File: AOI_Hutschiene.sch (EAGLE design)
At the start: 33 parts, among them IC1 l4940, SW1 EC12E_SW

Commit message: updated design
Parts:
- removed H5, H6, H7: MOUNT-PAD-ROUND3.2, holes:MOUNT-PAD-ROUND3.2
- removed SV3: (no value), con-lsta:FE05W
- added D1: 1N4148DO35-7, diode:1N4148DO35-7
- added R5, R6: 4k7, resistor:R-EU_0207/2V
- added R7, R8: 22k, resistor:R-EU_0207/10
- added SV5: (no value), con-lstb:MA04-1
- C3: value 1000uF -> 1mF
- F2: value FUSESH22,5 -> 100mA_or_smaller
- R1, R2: value (none) -> 180
- TR1: value 6v -> 6V, 300mA
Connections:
- net N$12 renamed DSS_VCC
- removed net REL_HEAT_2: U$1.A1
- removed net REL_MIX_2: U$1.A3
- net DISP_CLK_IN: now also SV5.4; no longer SV3.4
- net DISP_DATA_IN: now also SV5.3; no longer SV3.3
- net GND: now also IC2.I3, IC2.I4, IC2.I5, IC2.I6, IC2.I7, IC2.I8, R7.1, R8.1
- net GNDIO: now also SV5.1; no longer SV3.1
- net N$1: now also R5.2, R6.2
- net N$2: now also R5.1
- net N$3: now also R6.1
- net REL_HEAT_OUT: now also D1.A, R8.2
- net REL_MIX_OUT: now also D1.C, R7.2
- net VCCIO: now also SV5.2; no longer SV3.2
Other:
- note added: "1-2: always on"
- note added: "2-3 : auto"
- note added: "2-x : off"
- note added: "HMI"
- note added: "HMI Jack"
- note added: "Hutschienenmodul"
- note added: "Jack, LEDs, encoder, buzzer"
- note added: "Note: R3 inserted for current limitation in case of short circuit"
- note added: "Optional: D1 pulls heater input to zero if mixer is off => will prevent heating without mixer being in operation"
- note added: "VCC: 5V for logic/relais"
- note added: "VDD: 9V unregulated, selectable for relais output"
- note added: "arduino"
- note added: "both switches should be on-off-on type"
- note added: "holes"
- note added: "power supply"
- note added: "relais control"
- note added: "switches"
- note added: "temperature sensor interface"
- moved on the sheet: B1, C1, C2, C3, C4, F2, H1, H2, H3, H4, IC1, IC2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

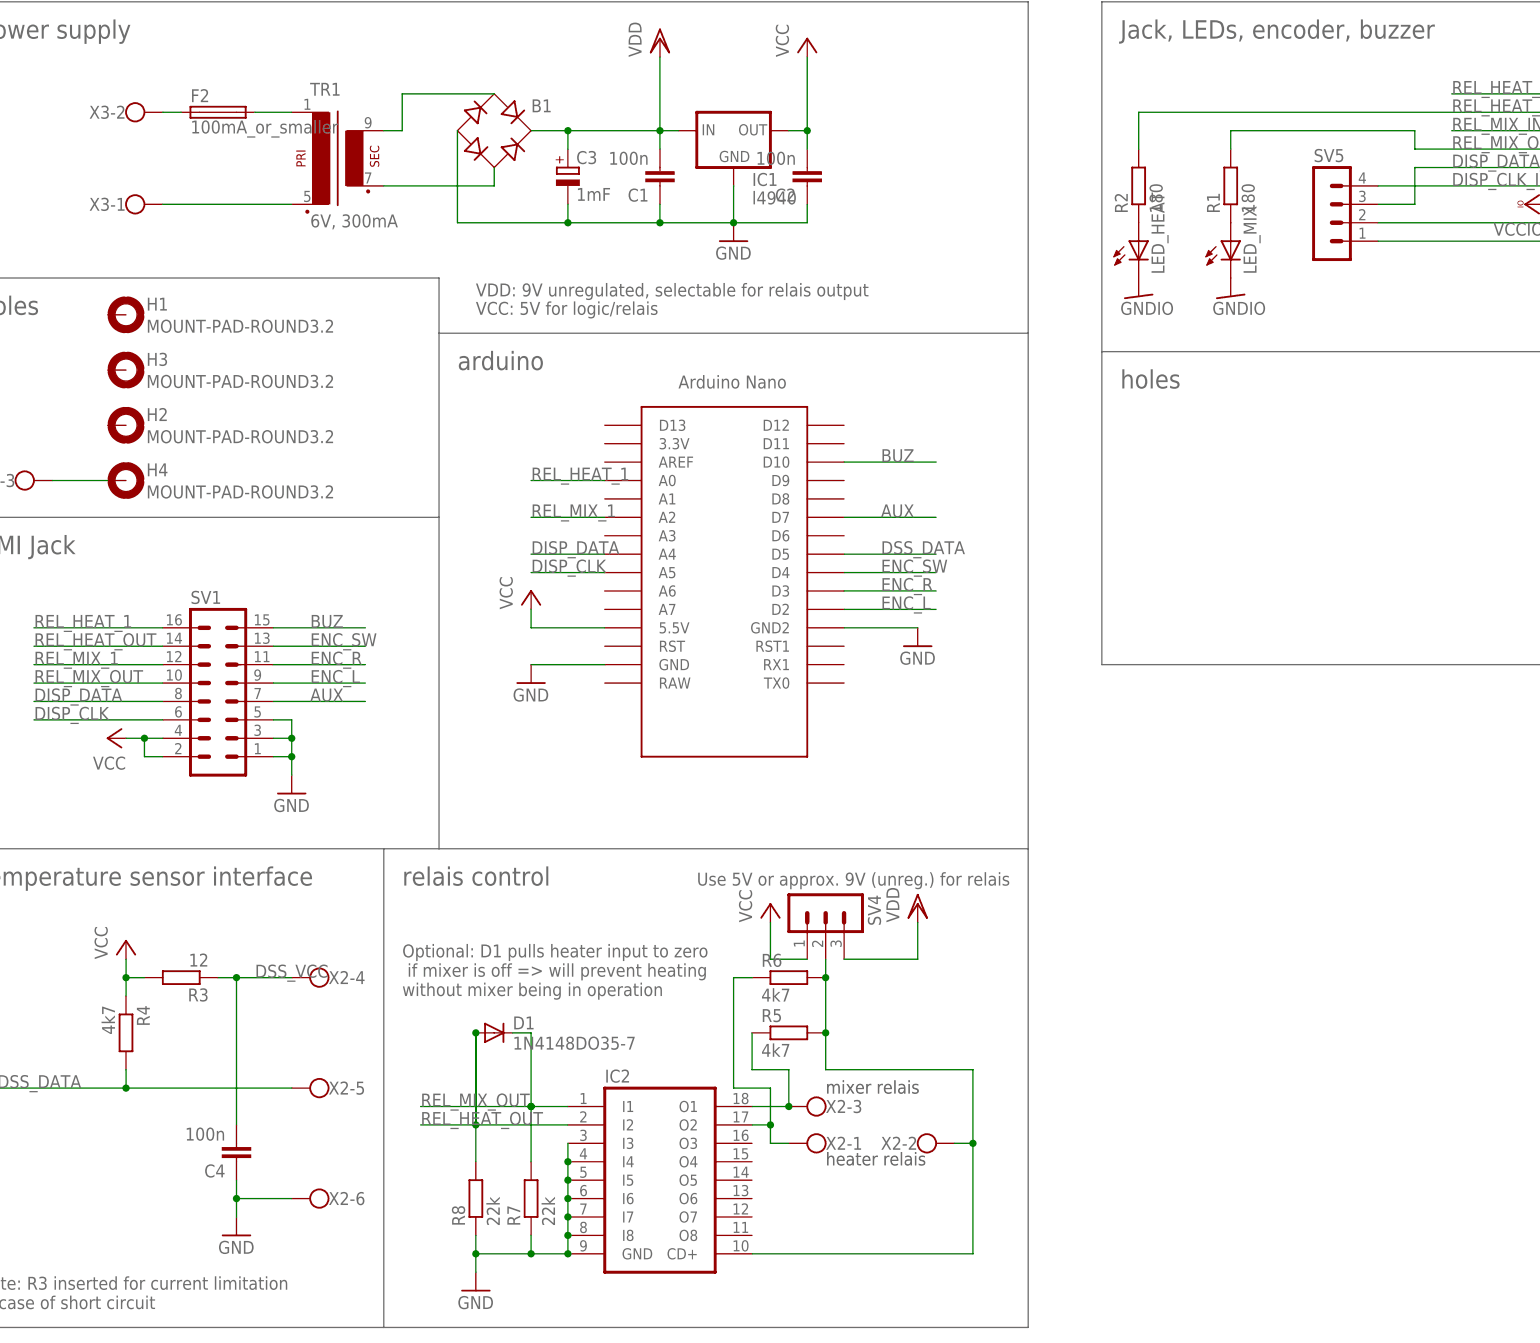
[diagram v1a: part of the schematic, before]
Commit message: Bugfixes to schematic and board (D1, R3/R4)
- D1: Wrong position. Declared as "dont use"
- R3/R4: Wrong silk screen position in PCB. Fixed by interchanging component names in schematic
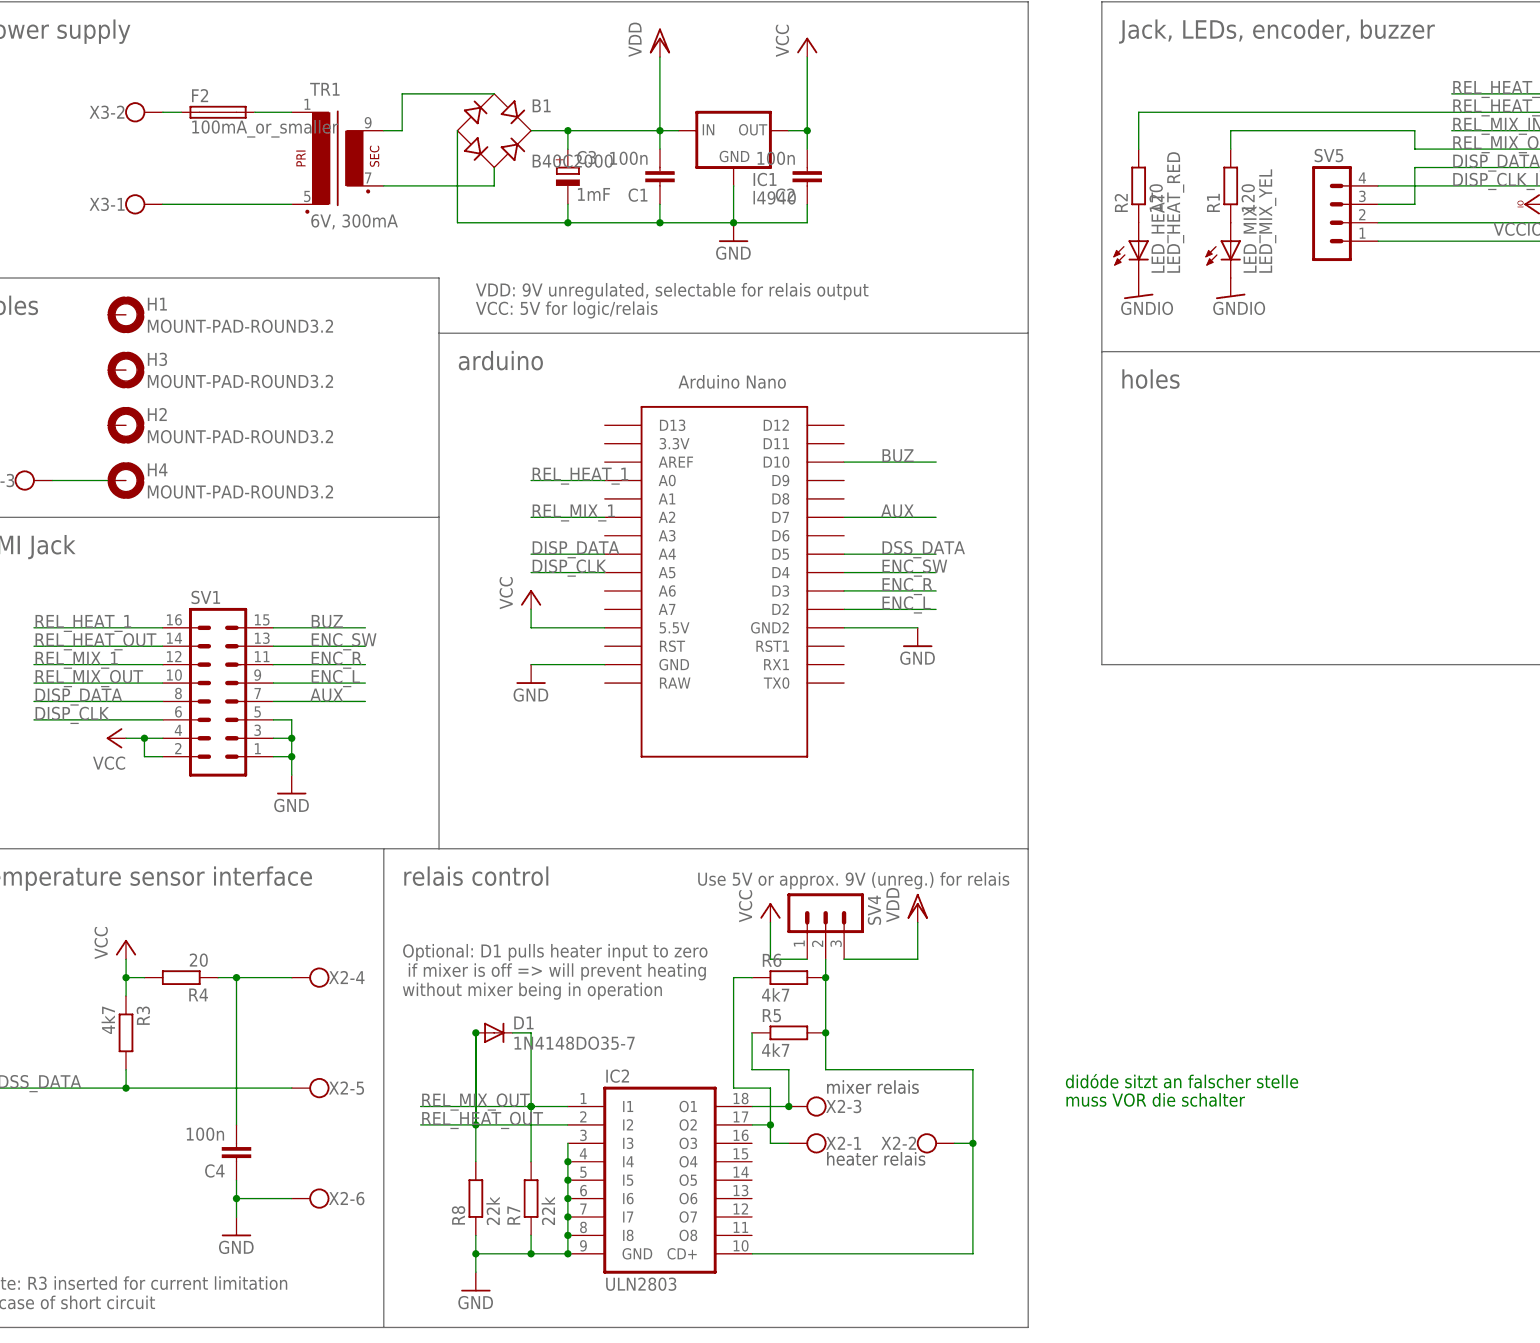
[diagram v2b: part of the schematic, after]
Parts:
- B1: value (none) -> B40C2000
- IC2: value (none) -> ULN2803
- LED_HEAT: value (none) -> LED_HEAT_RED
- LED_MIX: value (none) -> LED_MIX_YEL
- R1, R2: value 180 -> 120
- R3: value 12 -> 4k7
- R4: value 4k7 -> 20
- U$1: value NANO -> ArdNano_with_socket
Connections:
- removed net DSS_VCC: C4.2, R3.1, X2-4.KL
- new net N$12: C4.2, R4.1, X2-4.KL
- net DSS_DATA: now also R3.2; no longer R4.2
- net VCC: now also R3.1, R4.2; no longer R3.2, R4.1
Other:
- note added: "didóde sitzt an falscher stelle"
- note added: "muss VOR die schalter"
- moved on the sheet: R3, R4
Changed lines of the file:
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@@
 </classes>
 <parts>
-<part name="U$1" library="Arduino-clone" deviceset="NANO" device=""/>
+<part name="U$1" library="Arduino-clone" deviceset="NANO" device="" value="ArdNano_with_socket"/>
 <part name="SV1" library="con-ml" deviceset="ML16" device=""/>
-<part name="IC2" library="uln-udn" deviceset="ULN2803A" device=""/>
-<part name="R1" library="resistor" deviceset="R-EU_" device="0207/10" value="180"/>
+<part name="IC2" library="uln-udn" deviceset="ULN2803A" device="" value="ULN2803"/>
+<part name="R1" library="resistor" deviceset="R-EU_" device="0207/10" value="120"/>
 <part name="X2" library="con-wago-500" deviceset="W237-6" device=""/>
 <part name="TR1" library="trafo" deviceset="EI30-1" device="" value="6V, 300mA"/>
-<part name="B1" library="rectifier" deviceset="RB1A" device=""/>
+<part name="B1" library="rectifier" deviceset="RB1A" device="" value="B40C2000"/>
 <part name="C1" library="rcl" deviceset="C-EU" device="025_050-025X075" value="100n"/>
 <part name="C2" library="rcl" deviceset="C-EU" device="025_050-025X075" value="100n"/>
@@
 <part name="P+4" library="supply1" deviceset="VCC" device=""/>
 <part name="GND8" library="supply1" deviceset="GND" device=""/>
-<part name="R2" library="resistor" deviceset="R-EU_" device="0207/10" value="180"/>
-<part name="LED_HEAT" library="led" deviceset="LED" device="5MM"/>
-<part name="LED_MIX" library="led" deviceset="LED" device="5MM"/>
+<part name="R2" library="resistor" deviceset="R-EU_" device="0207/10" value="120"/>
+<part name="LED_HEAT" library="led" deviceset="LED" device="5MM" value="LED_HEAT_RED"/>
+<part name="LED_MIX" library="led" deviceset="LED" device="5MM" value="LED_MIX_YEL"/>
 <part name="GND9" library="supply1" deviceset="GNDIO" device=""/>
 <part name="GND10" library="supply1" deviceset="GNDIO" device=""/>
@@
 <part name="SV4" library="con-lstb" deviceset="MA03-1" device=""/>
 <part name="P+5" library="supply1" deviceset="VCC" device=""/>
-<part name="R3" library="resistor" deviceset="R-EU_" device="0207/10" value="12"/>
-<part name="R4" library="resistor" deviceset="R-EU_" device="0207/10" value="4k7"/>
+<part name="R4" library="resistor" deviceset="R-EU_" device="0207/10" value="20"/>
+<part name="R3" library="resistor" deviceset="R-EU_" device="0207/10" value="4k7"/>
 <part name="C4" library="rcl" deviceset="C-EU" device="025_050-025X075" value="100n"/>
 <part name="GND12" library="supply1" deviceset="GND" device=""/>
@@
  if mixer is off =&gt; will prevent heating
 without mixer being in operation</text>
+<text x="93.98" y="-55.88" size="1.778" layer="91">didóde sitzt an falscher stelle</text>
+<text x="93.98" y="-58.42" size="1.778" layer="91">muss VOR die schalter</text>
 </plain>
 <instances>
@@
 <instance part="SV4" gate="G$1" x="60.96" y="-30.48" rot="R270"/>
 <instance part="P+5" gate="VCC" x="-35.56" y="-35.56"/>
-<instance part="R3" gate="G$1" x="-27.94" y="-40.64" rot="R180"/>
-<instance part="R4" gate="G$1" x="-35.56" y="-48.26" rot="R270"/>
+<instance part="R4" gate="G$1" x="-27.94" y="-40.64" rot="R180"/>
+<instance part="R3" gate="G$1" x="-35.56" y="-48.26" rot="R270"/>
 <instance part="C4" gate="G$1" x="-20.32" y="-66.04" rot="R180"/>
 <instance part="GND12" gate="1" x="-20.32" y="-76.2"/>
@@
 <pinref part="X2" gate="-5" pin="KL"/>
 <wire x1="-12.7" y1="-55.88" x2="-35.56" y2="-55.88" width="0.1524" layer="91"/>
-<pinref part="R4" gate="G$1" pin="2"/>
+<pinref part="R3" gate="G$1" pin="2"/>
 <wire x1="-35.56" y1="-55.88" x2="-35.56" y2="-53.34" width="0.1524" layer="91"/>
 <wire x1="-35.56" y1="-55.88" x2="-53.34" y2="-55.88" width="0.1524" layer="91"/>
@@
 </segment>
 <segment>
-<pinref part="R4" gate="G$1" pin="1"/>
+<pinref part="R3" gate="G$1" pin="1"/>
 <pinref part="P+5" gate="VCC" pin="VCC"/>
 <wire x1="-35.56" y1="-43.18" x2="-35.56" y2="-40.64" width="0.1524" layer="91"/>
-<pinref part="R3" gate="G$1" pin="2"/>
+<pinref part="R4" gate="G$1" pin="2"/>
 <wire x1="-35.56" y1="-40.64" x2="-35.56" y2="-38.1" width="0.1524" layer="91"/>
 <wire x1="-33.02" y1="-40.64" x2="-35.56" y2="-40.64" width="0.1524" layer="91"/>
@@
 </segment>
 </net>
-<net name="AUX" class="0">
-<segment>
-<pinref part="U$1" gate="G$1" pin="D7"/>
-<wire x1="63.5" y1="22.86" x2="76.2" y2="22.86" width="0.1524" layer="91"/>
-<label x="68.58" y="22.86" size="1.778" layer="95"/>
-</segment>
-<segment>
-<pinref part="SV1" gate="1" pin="7"/>
-<wire x1="-15.24" y1="-2.54" x2="-2.54" y2="-2.54" width="0.1524" layer="91"/>
-<label x="-10.16" y="-2.54" size="1.778" layer="95"/>
-</segment>
-</net>
-<net name="AUX_IO" class="0">
-<segment>
-<pinref part="SV2" gate="1" pin="7"/>
-<wire x1="180.34" y1="71.12" x2="198.12" y2="71.12" width="0.1524" layer="91"/>
-<label x="185.42" y="71.12" size="1.778" layer="95"/>
-</segment>
-</net>
-<net name="N$7" class="0">
-<segment>
-<pinref part="X3" gate="-2" pin="KL"/>
-<wire x1="-30.48" y1="78.74" x2="-27.94" y2="78.74" width="0.1524" layer="91"/>
-<pinref part="F2" gate="G$1" pin="1"/>
-</segment>
-</net>
-<net name="N$8" class="0">
-<segment>
-<pinref part="X3" gate="-1" pin="KL"/>
-<pinref part="TR1" gate="1" pin="P2"/>
-<wire x1="-30.48" y1="66.04" x2="-12.7" y2="66.04" width="0.1524" layer="91"/>
-</segment>
-</net>
-<net name="N$98" class="0">
-<segment>
-<pinref part="X3" gate="-3" pin="KL"/>
-<pinref part="H4" gate="G$1" pin="MOUNT"/>
-<wire x1="-38.1" y1="27.94" x2="-45.72" y2="27.94" width="0.1524" layer="91"/>
-</segment>
-</net>
-<net name="DSS_VCC" class="0">
-<segment>
-<pinref part="R3" gate="G$1" pin="1"/>
+<net name="N$12" class="0">
+<segment>
+<pinref part="R4" gate="G$1" pin="1"/>
 <pinref part="X2" gate="-4" pin="KL"/>
 <wire x1="-22.86" y1="-40.64" x2="-20.32" y2="-40.64" width="0.1524" layer="91"/>
@@
 <wire x1="-20.32" y1="-60.96" x2="-20.32" y2="-40.64" width="0.1524" layer="91"/>
 <junction x="-20.32" y="-40.64"/>
-<label x="-17.78" y="-40.64" size="1.778" layer="95"/>
-</segment>
-</net>
+</segment>
+</net>
+<net name="AUX" class="0">
+<segment>
+<pinref part="U$1" gate="G$1" pin="D7"/>
+<wire x1="63.5" y1="22.86" x2="76.2" y2="22.86" width="0.1524" layer="91"/>
+<label x="68.58" y="22.86" size="1.778" layer="95"/>
+</segment>
+<segment>
+<pinref part="SV1" gate="1" pin="7"/>
+<wire x1="-15.24" y1="-2.54" x2="-2.54" y2="-2.54" width="0.1524" layer="91"/>
+<label x="-10.16" y="-2.54" size="1.778" layer="95"/>
+</segment>
+</net>
+<net name="AUX_IO" class="0">
+<segment>
+<pinref part="SV2" gate="1" pin="7"/>
+<wire x1="180.34" y1="71.12" x2="198.12" y2="71.12" width="0.1524" layer="91"/>
+<label x="185.42" y="71.12" size="1.778" layer="95"/>
+</segment>
+</net>
+<net name="N$7" class="0">
+<segment>
+<pinref part="X3" gate="-2" pin="KL"/>
+<wire x1="-30.48" y1="78.74" x2="-27.94" y2="78.74" width="0.1524" layer="91"/>
+<pinref part="F2" gate="G$1" pin="1"/>
+</segment>
+</net>
+<net name="N$8" class="0">
+<segment>
+<pinref part="X3" gate="-1" pin="KL"/>
+<pinref part="TR1" gate="1" pin="P2"/>
+<wire x1="-30.48" y1="66.04" x2="-12.7" y2="66.04" width="0.1524" layer="91"/>
+</segment>
+</net>
+<net name="N$98" class="0">
+<segment>
+<pinref part="X3" gate="-3" pin="KL"/>
+<pinref part="H4" gate="G$1" pin="MOUNT"/>
+<wire x1="-38.1" y1="27.94" x2="-45.72" y2="27.94" width="0.1524" layer="91"/>
+</segment>
+</net>
